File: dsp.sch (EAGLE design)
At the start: 117 parts, among them IC1 OPA2134P, IC2 OPA2134P, Q1 BC550B, U1 STM32F405RGT6, U2 CODECODER-WM8731SEDS/V(SSOP28), U4 LM2575HVS-3.3/NOPB, X1 ABLS-8.000MHZ-B4-T

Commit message: fixed mclk and uart connections
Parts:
- added R45, R46: 10k, dan:R-US_0309/V
- C21, C22: value 2.2u -> 1u
- C24, C25: value 1u -> .22u
- C26, C27, C28, C29: value 220p -> 180p
- R43, R44: value 4.7k -> 47k
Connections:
- new net N$51: R45.1, U$3.SW1
- new net N$52: R46.1, U$4.SW1
- net 4.5V: now also DRYG$1.A, DRYG$2.A, WETG$1.A, WETG$2.A
- net GND: no longer DRYG$1.A, DRYG$2.A, WETG$1.A, WETG$2.A
- net MCLK: now also U1.PA3/USART2_RX; no longer U1.PC6
- net N$50: now also U1.PA10; no longer U1.PA3/USART2_RX
- net N$8: now also U1.PA9; no longer U1.PA2/USART2_TX
- net SWITCH1: now also R45.2; no longer U$3.SW1
- net SWITCH2: now also R46.2; no longer U$4.SW1
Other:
- moved on the sheet: C15, C16, C32, C33, LED2, PARAM1, PARAM2, R42, R43, R44, R8, RX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

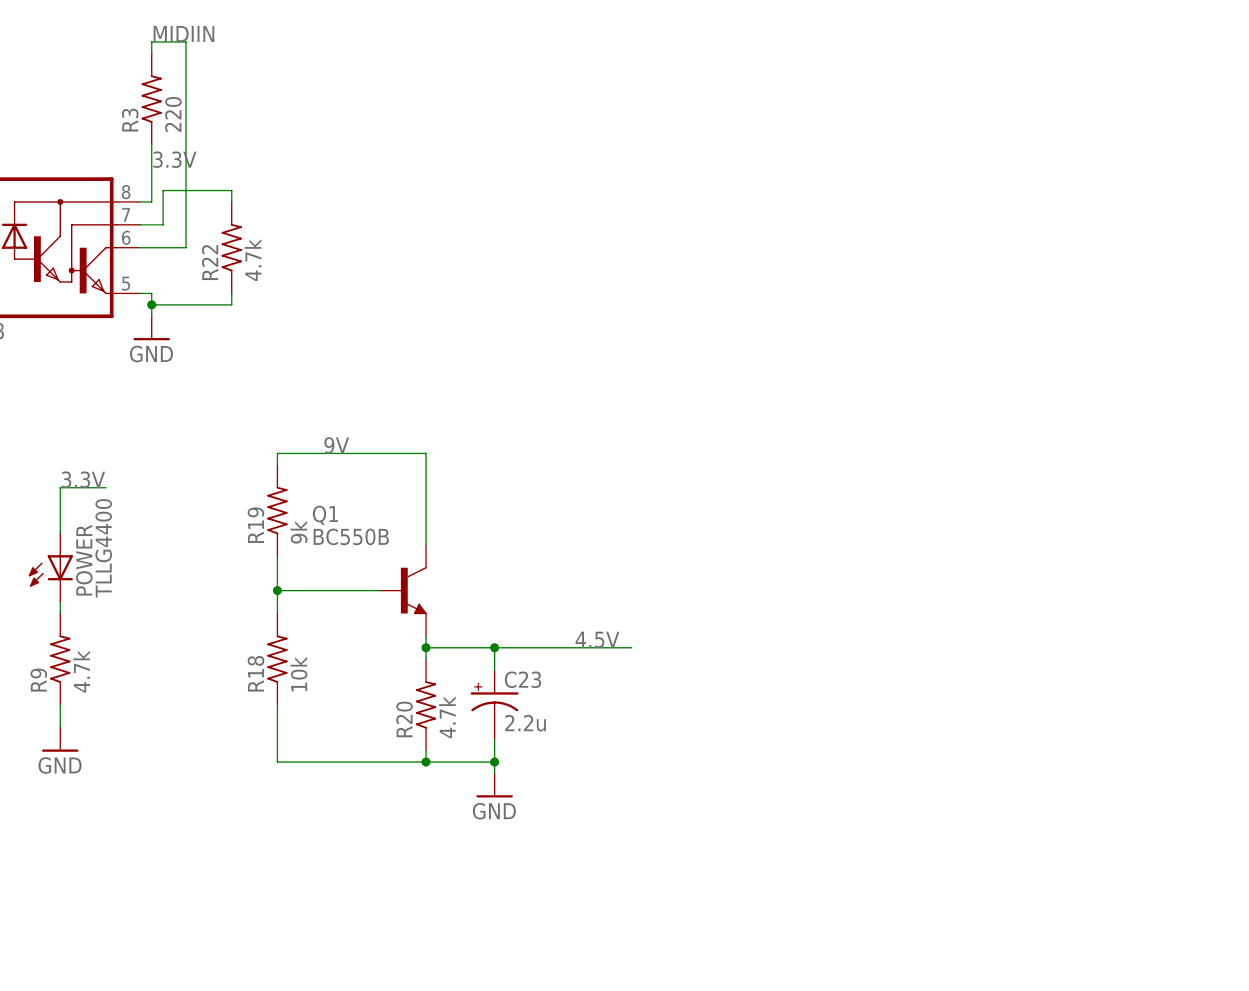
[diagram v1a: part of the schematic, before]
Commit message: changed virtual ground to an op amp buffer
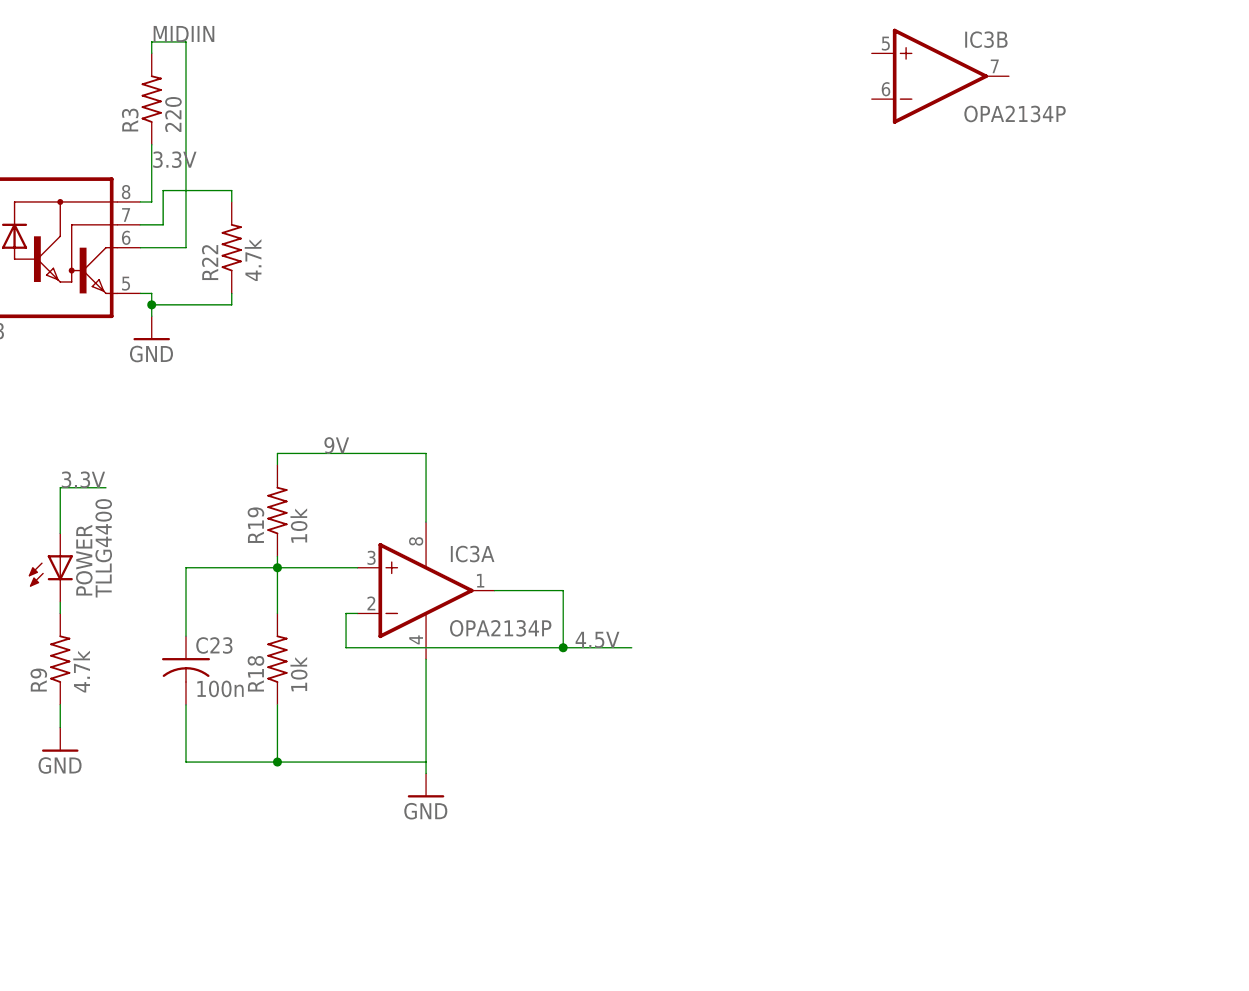
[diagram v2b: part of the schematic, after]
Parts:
- removed Q1: BC550B, dan:BC550B
- removed R20: 4.7k, dan:R-US_0309/V
- added IC3: OPA2134P, dan:OPA2134P
- C23: value 2.2u -> 100n; device dan:CPOL-USE2.5-7 -> dan:C-US050-025X075
- R19: value 9k -> 10k
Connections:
- net 4.5V: now also IC3A.-IN, IC3A.OUT; no longer C23.+, Q1.E, R20.2
- net 9V: now also IC3P.V+; no longer Q1.C
- net GND: now also C23.2, IC3P.V-; no longer C23.-, R20.1
- net N$20: now also C23.1, IC3A.+IN; no longer Q1.B
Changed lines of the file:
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@@
 <part name="IC1" library="dan" deviceset="OPA2134" device="P"/>
 <part name="R18" library="dan" deviceset="R-US_" device="0309/V" value="10k"/>
-<part name="R19" library="dan" deviceset="R-US_" device="0309/V" value="9k"/>
-<part name="R20" library="dan" deviceset="R-US_" device="0309/V" value="4.7k"/>
+<part name="R19" library="dan" deviceset="R-US_" device="0309/V" value="10k"/>
 <part name="GND21" library="dan" deviceset="GND" device=""/>
 <part name="R21" library="dan" deviceset="R-US_" device="0309/V" value="47k"/>
 <part name="R23" library="dan" deviceset="R-US_" device="0309/V" value="47k"/>
 <part name="IC2" library="dan" deviceset="OPA2134" device="P"/>
-<part name="C23" library="dan" deviceset="CPOL-US" device="E2.5-7" value="2.2u"/>
 <part name="GND22" library="dan" deviceset="GND" device=""/>
 <part name="GND17" library="dan" deviceset="GND" device=""/>
@@
 <part name="GND33" library="dan" deviceset="GND" device=""/>
 <part name="R1" library="dan" deviceset="R-US_" device="0309/V" value="10"/>
-<part name="Q1" library="dan" deviceset="BC550*" device="" technology="B"/>
 <part name="U$3" library="dan" deviceset="CHERRY-MX-LED" device=""/>
 <part name="U$4" library="dan" deviceset="CHERRY-MX-LED" device=""/>
@@
 <part name="R45" library="dan" deviceset="R-US_" device="0309/V" value="10k"/>
 <part name="R46" library="dan" deviceset="R-US_" device="0309/V" value="10k"/>
+<part name="IC3" library="dan" deviceset="OPA2134" device="P"/>
+<part name="C23" library="dan" deviceset="C-US" device="050-025X075" value="100n"/>
 </parts>
 <sheets>
@@
 <instance part="R18" gate="G$1" x="104.14" y="166.37" rot="R90"/>
 <instance part="R19" gate="G$1" x="104.14" y="182.88" rot="R90"/>
-<instance part="R20" gate="G$1" x="120.65" y="161.29" rot="R90"/>
 <instance part="GND21" gate="1" x="292.1" y="199.39"/>
 <instance part="R21" gate="G$1" x="297.18" y="127"/>
@@
 <instance part="IC2" gate="B" x="270.51" y="-10.16" rot="R180"/>
 <instance part="IC2" gate="P" x="271.78" y="45.72" rot="R180"/>
-<instance part="C23" gate="G$1" x="128.27" y="162.56"/>
-<instance part="GND22" gate="1" x="128.27" y="151.13"/>
+<instance part="GND22" gate="1" x="120.65" y="151.13"/>
 <instance part="GND17" gate="1" x="264.16" y="54.61"/>
 <instance part="R25" gate="G$1" x="267.97" y="63.5"/>
@@
 <instance part="GND33" gate="1" x="-3.81" y="162.56"/>
 <instance part="R1" gate="G$1" x="-36.83" y="175.26" rot="R180"/>
-<instance part="Q1" gate="G$1" x="118.11" y="173.99"/>
 <instance part="U$3" gate="G$1" x="-63.5" y="132.08" rot="R90"/>
 <instance part="U$4" gate="G$1" x="-46.99" y="132.08" rot="R90"/>
@@
 <instance part="R45" gate="G$1" x="-66.04" y="111.76" rot="R270"/>
 <instance part="R46" gate="G$1" x="-49.53" y="111.76" rot="R270"/>
+<instance part="IC3" gate="A" x="120.65" y="173.99"/>
+<instance part="IC3" gate="B" x="177.8" y="231.14"/>
+<instance part="IC3" gate="P" x="120.65" y="173.99"/>
+<instance part="C23" gate="G$1" x="93.98" y="166.37"/>
 </instances>
 <busses>
@@
 </segment>
 <segment>
-<wire x1="120.65" y1="179.07" x2="120.65" y2="189.23" width="0.1524" layer="91"/>
 <pinref part="R19" gate="G$1" pin="2"/>
 <wire x1="120.65" y1="189.23" x2="104.14" y2="189.23" width="0.1524" layer="91"/>
 <wire x1="104.14" y1="189.23" x2="104.14" y2="187.96" width="0.1524" layer="91"/>
 <label x="109.22" y="189.23" size="1.778" layer="95"/>
-<pinref part="Q1" gate="G$1" pin="C"/>
+<pinref part="IC3" gate="P" pin="V+"/>
+<wire x1="120.65" y1="181.61" x2="120.65" y2="189.23" width="0.1524" layer="91"/>
 </segment>
 <segment>
@@
 </segment>
 <segment>
-<pinref part="R18" gate="G$1" pin="1"/>
-<pinref part="R20" gate="G$1" pin="1"/>
-<wire x1="120.65" y1="156.21" x2="120.65" y2="154.94" width="0.1524" layer="91"/>
-<wire x1="120.65" y1="154.94" x2="104.14" y2="154.94" width="0.1524" layer="91"/>
-<wire x1="104.14" y1="154.94" x2="104.14" y2="161.29" width="0.1524" layer="91"/>
-<pinref part="C23" gate="G$1" pin="-"/>
-<wire x1="128.27" y1="157.48" x2="128.27" y2="154.94" width="0.1524" layer="91"/>
-<wire x1="128.27" y1="154.94" x2="120.65" y2="154.94" width="0.1524" layer="91"/>
-<junction x="120.65" y="154.94"/>
-<pinref part="GND22" gate="1" pin="GND"/>
-<wire x1="128.27" y1="153.67" x2="128.27" y2="154.94" width="0.1524" layer="91"/>
-<junction x="128.27" y="154.94"/>
-</segment>
-<segment>
 <pinref part="IC2" gate="P" pin="V-"/>
 <wire x1="271.78" y1="53.34" x2="271.78" y2="58.42" width="0.1524" layer="91"/>
@@
 <pinref part="GND42" gate="1" pin="GND"/>
 <wire x1="-66.04" y1="87.63" x2="-66.04" y2="88.9" width="0.1524" layer="91"/>
+</segment>
+<segment>
+<pinref part="IC3" gate="P" pin="V-"/>
+<pinref part="GND22" gate="1" pin="GND"/>
+<wire x1="120.65" y1="153.67" x2="120.65" y2="154.94" width="0.1524" layer="91"/>
+<pinref part="R18" gate="G$1" pin="1"/>
+<wire x1="120.65" y1="154.94" x2="120.65" y2="166.37" width="0.1524" layer="91"/>
+<wire x1="104.14" y1="154.94" x2="104.14" y2="161.29" width="0.1524" layer="91"/>
+<wire x1="104.14" y1="154.94" x2="120.65" y2="154.94" width="0.1524" layer="91"/>
+<pinref part="C23" gate="G$1" pin="2"/>
+<wire x1="93.98" y1="161.29" x2="93.98" y2="154.94" width="0.1524" layer="91"/>
+<wire x1="93.98" y1="154.94" x2="104.14" y2="154.94" width="0.1524" layer="91"/>
+<junction x="104.14" y="154.94"/>
 </segment>
 </net>
@@
 <segment>
 <pinref part="R18" gate="G$1" pin="2"/>
-<wire x1="115.57" y1="173.99" x2="104.14" y2="173.99" width="0.1524" layer="91"/>
-<wire x1="104.14" y1="173.99" x2="104.14" y2="171.45" width="0.1524" layer="91"/>
 <pinref part="R19" gate="G$1" pin="1"/>
-<wire x1="104.14" y1="177.8" x2="104.14" y2="173.99" width="0.1524" layer="91"/>
-<junction x="104.14" y="173.99"/>
-<pinref part="Q1" gate="G$1" pin="B"/>
+<wire x1="104.14" y1="177.8" x2="104.14" y2="176.53" width="0.1524" layer="91"/>
+<pinref part="IC3" gate="A" pin="+IN"/>
+<wire x1="104.14" y1="176.53" x2="104.14" y2="171.45" width="0.1524" layer="91"/>
+<wire x1="113.03" y1="176.53" x2="104.14" y2="176.53" width="0.1524" layer="91"/>
+<junction x="104.14" y="176.53"/>
+<pinref part="C23" gate="G$1" pin="1"/>
+<wire x1="93.98" y1="168.91" x2="93.98" y2="176.53" width="0.1524" layer="91"/>
+<wire x1="93.98" y1="176.53" x2="104.14" y2="176.53" width="0.1524" layer="91"/>
 </segment>
 </net>
 <net name="4.5V" class="0">
 <segment>
-<pinref part="R20" gate="G$1" pin="2"/>
-<wire x1="120.65" y1="166.37" x2="120.65" y2="167.64" width="0.1524" layer="91"/>
-<wire x1="120.65" y1="167.64" x2="120.65" y2="168.91" width="0.1524" layer="91"/>
-<wire x1="120.65" y1="167.64" x2="128.27" y2="167.64" width="0.1524" layer="91"/>
-<junction x="120.65" y="167.64"/>
 <label x="137.16" y="167.64" size="1.778" layer="95"/>
-<pinref part="C23" gate="G$1" pin="+"/>
-<wire x1="128.27" y1="167.64" x2="143.51" y2="167.64" width="0.1524" layer="91"/>
-<wire x1="128.27" y1="165.1" x2="128.27" y2="167.64" width="0.1524" layer="91"/>
-<junction x="128.27" y="167.64"/>
-<pinref part="Q1" gate="G$1" pin="E"/>
-</segment>
-<segment>
+<wire x1="135.89" y1="167.64" x2="143.51" y2="167.64" width="0.1524" layer="91"/>
+<pinref part="IC3" gate="A" pin="-IN"/>
+<wire x1="113.03" y1="171.45" x2="111.76" y2="171.45" width="0.1524" layer="91"/>
+<wire x1="111.76" y1="171.45" x2="111.76" y2="167.64" width="0.1524" layer="91"/>
+<wire x1="111.76" y1="167.64" x2="135.89" y2="167.64" width="0.1524" layer="91"/>
+<wire x1="135.89" y1="167.64" x2="135.89" y2="173.99" width="0.1524" layer="91"/>
+<pinref part="IC3" gate="A" pin="OUT"/>
+<wire x1="135.89" y1="173.99" x2="128.27" y2="173.99" width="0.1524" layer="91"/>
+<junction x="135.89" y="167.64"/>
+</segment>
+<segment>
